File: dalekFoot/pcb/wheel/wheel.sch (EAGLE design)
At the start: 79 parts, among them IC1 LM1117MP-3.3, IC2 LM1117MP-3.3, IC3 LM1117MP-3.3, IC4 4051D, IC5 4051D, IC6 LM1117MP-3.3, K1 12X12-TACTILE, K2 12X12-TACTILE, K3 12X12-TACTILE, K4 12X12-TACTILE, K5 12X12-TACTILE, U1 TB6612FNG(O,C,8,EL, U2 SS8050-SOT-23, U3 SS8050-SOT-23, U4 SS8050-SOT-23, U5 TB6612FNG(O,C,8,EL, U6 TB6612FNG(O,C,8,EL

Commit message: add standalone usart port
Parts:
- added JP8: (no value), pinhead:PINHD-1X4
- added R36: (no value), rcl:R-EU_R0402
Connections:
- new net N$3: JP8.1, R36.2
- new net VCC-DIGITAL: B1.P$+, C2.+, IC1.OUT, JP5.1, JP5.2, JP6.1, JP6.2, LED1.A, LED2.A, R27.1, R28.1, R36.1, U$1.P$3V3, U1.STBY, U1.VCC, U5.STBY, U5.VCC, U6.STBY, U6.VCC
- net DGND: now also JP8.4
- net USART_RX: now also JP8.3
- net USART_TX: now also JP8.2
- net VCC-IRT: no longer B1.P$+, C2.+, IC1.OUT, JP5.1, JP5.2, JP6.1, JP6.2, LED1.A, LED2.A, R27.1, R28.1, U$1.P$3V3, U1.STBY, U1.VCC, U5.STBY, U5.VCC, U6.STBY, U6.VCC
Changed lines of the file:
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@@
 <setting verticaltext="up"/>
 </settings>
-<grid distance="0.1" unitdist="inch" unit="inch" style="lines" multiple="1" display="yes" altdistance="0.01" altunitdist="inch" altunit="inch"/>
+<grid distance="0.1" unitdist="inch" unit="inch" style="lines" multiple="1" display="no" altdistance="0.01" altunitdist="inch" altunit="inch"/>
 <layers>
 <layer number="1" name="Top" color="4" fill="1" visible="no" active="no"/>
@@
 <part name="U$2" library="hqc" deviceset="BATTERY-10A" device=""/>
 <part name="SUPPLY38" library="supply2" deviceset="DGND" device=""/>
+<part name="JP8" library="pinhead" deviceset="PINHD-1X4" device=""/>
+<part name="SUPPLY39" library="supply2" deviceset="DGND" device=""/>
+<part name="R36" library="rcl" deviceset="R-EU_" device="R0402"/>
 </parts>
 <sheets>
@@
 <instance part="U$2" gate="G$1" x="38.1" y="25.4"/>
 <instance part="SUPPLY38" gate="G$1" x="38.1" y="15.24"/>
+<instance part="JP8" gate="A" x="335.28" y="223.52"/>
+<instance part="SUPPLY39" gate="G$1" x="325.12" y="215.9"/>
+<instance part="R36" gate="G$1" x="312.42" y="228.6"/>
 </instances>
 <busses>
@@
 <wire x1="38.1" y1="20.32" x2="38.1" y2="17.78" width="0.1524" layer="91"/>
 </segment>
+<segment>
+<pinref part="SUPPLY39" gate="G$1" pin="DGND"/>
+<wire x1="325.12" y1="218.44" x2="325.12" y2="220.98" width="0.1524" layer="91"/>
+<pinref part="JP8" gate="A" pin="4"/>
+<wire x1="325.12" y1="220.98" x2="332.74" y2="220.98" width="0.1524" layer="91"/>
+</segment>
 </net>
 <net name="BAT+" class="0">
@@
 </segment>
 </net>
-<net name="VCC-IRT" class="0">
+<net name="VCC-DIGITAL" class="0">
 <segment>
 <pinref part="IC1" gate="G$1" pin="OUT"/>
@@
 </segment>
 <segment>
-<pinref part="IC6" gate="G$1" pin="OUT"/>
-<wire x1="162.56" y1="81.28" x2="170.18" y2="81.28" width="0.1524" layer="91"/>
-<pinref part="C9" gate="G$1" pin="+"/>
-<wire x1="170.18" y1="81.28" x2="182.88" y2="81.28" width="0.1524" layer="91"/>
-<wire x1="170.18" y1="76.2" x2="170.18" y2="81.28" width="0.1524" layer="91"/>
-<junction x="170.18" y="81.28"/>
-<label x="177.8" y="81.28" size="1.778" layer="95"/>
-</segment>
-<segment>
-<pinref part="R35" gate="G$1" pin="P$1"/>
-<wire x1="137.16" y1="38.1" x2="149.86" y2="38.1" width="0.1524" layer="91"/>
-<label x="134.62" y="38.1" size="1.778" layer="95"/>
+<wire x1="307.34" y1="228.6" x2="289.56" y2="228.6" width="0.1524" layer="91"/>
+<label x="289.56" y="228.6" size="1.778" layer="95"/>
+<pinref part="R36" gate="G$1" pin="1"/>
 </segment>
 </net>
@@
 <label x="274.32" y="259.08" size="1.778" layer="95"/>
 </segment>
+<segment>
+<pinref part="JP8" gate="A" pin="2"/>
+<wire x1="314.96" y1="226.06" x2="332.74" y2="226.06" width="0.1524" layer="91"/>
+<label x="314.96" y="226.06" size="1.778" layer="95"/>
+</segment>
 </net>
 <net name="USART_RX" class="0">
@@
 <label x="274.32" y="256.54" size="1.778" layer="95"/>
 </segment>
-</net>
+<segment>
+<pinref part="JP8" gate="A" pin="3"/>
+<wire x1="332.74" y1="223.52" x2="314.96" y2="223.52" width="0.1524" layer="91"/>
+<label x="314.96" y="223.52" size="1.778" layer="95"/>
+</segment>
+</net>
+<net name="N$3" class="0">
+<segment>
+<pinref part="JP8" gate="A" pin="1"/>
+<wire x1="332.74" y1="228.6" x2="317.5" y2="228.6" width="0.1524" layer="91"/>
+<pinref part="R36" gate="G$1" pin="2"/>
+</segment>
+</net>
+<net name="VCC-IRT" class="0">
+<segment>
+<pinref part="IC6" gate="G$1" pin="OUT"/>
+<wire x1="162.56" y1="81.28" x2="170.18" y2="81.28" width="0.1524" layer="91"/>
+<pinref part="C9" gate="G$1" pin="+"/>
+<wire x1="170.18" y1="81.28" x2="182.88" y2="81.28" width="0.1524" layer="91"/>
+<wire x1="170.18" y1="76.2" x2="170.18" y2="81.28" width="0.1524" layer="91"/>
+<junction x="170.18" y="81.28"/>
+<label x="177.8" y="81.28" size="1.778" layer="95"/>
+</segment>
+<segment>
+<pinref part="R35" gate="G$1" pin="P$1"/>
+<wire x1="137.16" y1="38.1" x2="149.86" y2="38.1" width="0.1524" layer="91"/>
+<label x="134.62" y="38.1" size="1.778" layer="95"/>
+</segment>
+</net>

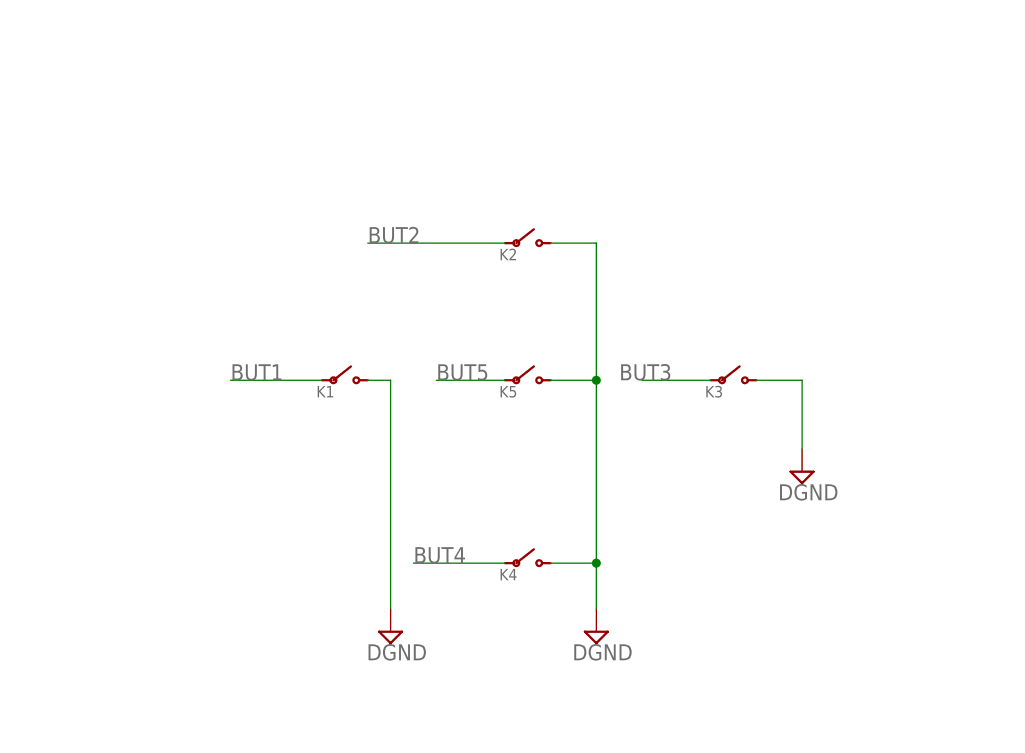
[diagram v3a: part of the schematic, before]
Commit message: place the parts in pcb, ready to route lines
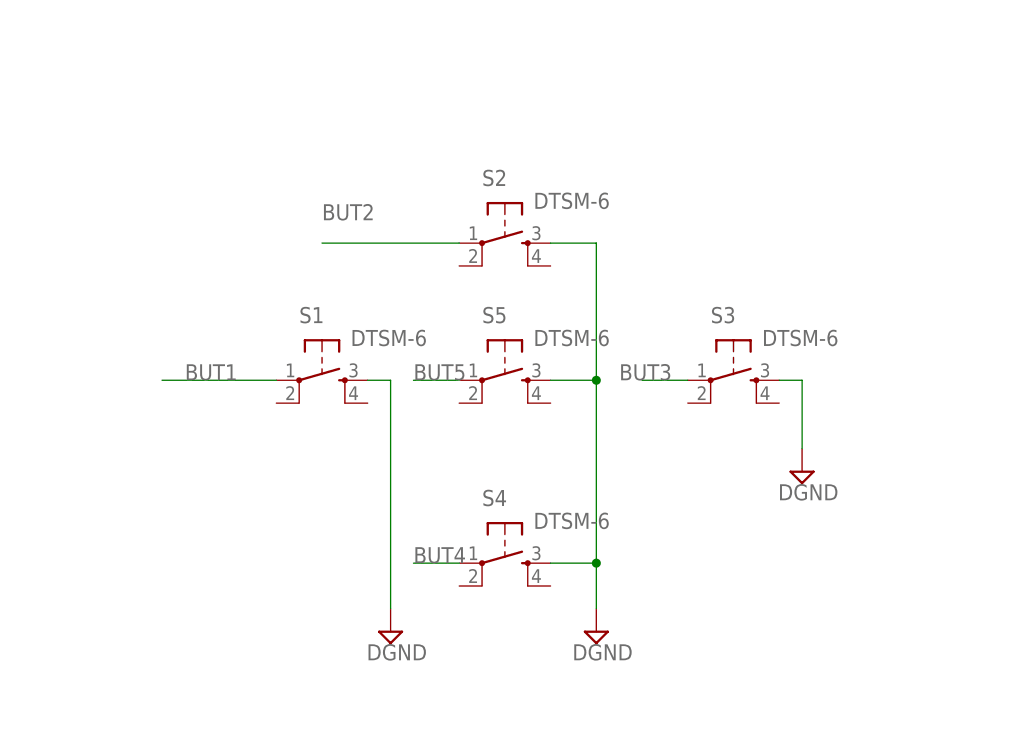
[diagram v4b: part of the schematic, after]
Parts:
- removed K1, K2, K3, K4, K5: 12X12-TACTILE, hqc:12X12-TACTILE
- added S1, S2, S3, S4, S5: DTSM-6, switch-tact:DTSM-6
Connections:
- net BUT1: now also S1.1; no longer K1.P$1
- net BUT2: now also S2.1; no longer K2.P$1
- net BUT3: now also S3.1; no longer K3.P$1
- net BUT4: now also S4.1; no longer K4.P$1
- net BUT5: now also S5.1; no longer K5.P$1
- net DGND: now also S1.3, S2.3, S3.3, S4.3, S5.3; no longer K1.P$2, K2.P$2, K3.P$2, K4.P$2, K5.P$2
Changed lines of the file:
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@@
 <setting verticaltext="up"/>
 </settings>
-<grid distance="0.1" unitdist="inch" unit="inch" style="lines" multiple="1" display="no" altdistance="0.01" altunitdist="inch" altunit="inch"/>
+<grid distance="0.1" unitdist="inch" unit="mil" style="lines" multiple="1" display="yes" altdistance="0.01" altunitdist="inch" altunit="inch"/>
 <layers>
 <layer number="1" name="Top" color="4" fill="1" visible="no" active="no"/>
@@
 <part name="J2" library="hqc" deviceset="KF250-2X12P" device=""/>
 <part name="SUPPLY30" library="supply2" deviceset="DGND" device=""/>
-<part name="K1" library="hqc" deviceset="12X12-TACTILE" device=""/>
-<part name="K2" library="hqc" deviceset="12X12-TACTILE" device=""/>
-<part name="K3" library="hqc" deviceset="12X12-TACTILE" device=""/>
-<part name="K4" library="hqc" deviceset="12X12-TACTILE" device=""/>
-<part name="K5" library="hqc" deviceset="12X12-TACTILE" device=""/>
 <part name="SUPPLY31" library="supply2" deviceset="DGND" device=""/>
 <part name="SUPPLY32" library="supply2" deviceset="DGND" device=""/>
@@
 <part name="SUPPLY39" library="supply2" deviceset="DGND" device=""/>
 <part name="R36" library="rcl" deviceset="R-EU_" device="R0402"/>
+<part name="S1" library="switch-tact" deviceset="DTSM-6" device=""/>
+<part name="S2" library="switch-tact" deviceset="DTSM-6" device=""/>
+<part name="S3" library="switch-tact" deviceset="DTSM-6" device=""/>
+<part name="S4" library="switch-tact" deviceset="DTSM-6" device=""/>
+<part name="S5" library="switch-tact" deviceset="DTSM-6" device=""/>
 </parts>
 <sheets>
@@
 <instance part="J2" gate="G$1" x="365.76" y="596.9" rot="R270"/>
 <instance part="SUPPLY30" gate="G$1" x="353.06" y="568.96"/>
-<instance part="K1" gate="G$1" x="78.74" y="375.92"/>
-<instance part="K2" gate="G$1" x="99.06" y="391.16"/>
-<instance part="K3" gate="G$1" x="121.92" y="375.92"/>
-<instance part="K4" gate="G$1" x="99.06" y="355.6"/>
-<instance part="K5" gate="G$1" x="99.06" y="375.92"/>
 <instance part="SUPPLY31" gate="G$1" x="106.68" y="347.98"/>
 <instance part="SUPPLY32" gate="G$1" x="83.82" y="347.98"/>
@@
 <instance part="SUPPLY39" gate="G$1" x="325.12" y="215.9"/>
 <instance part="R36" gate="G$1" x="312.42" y="228.6"/>
+<instance part="S1" gate="G$1" x="76.2" y="375.92" rot="R270"/>
+<instance part="S2" gate="G$1" x="96.52" y="391.16" rot="R270"/>
+<instance part="S3" gate="G$1" x="121.92" y="375.92" rot="R270"/>
+<instance part="S4" gate="G$1" x="96.52" y="355.6" rot="R270"/>
+<instance part="S5" gate="G$1" x="96.52" y="375.92" rot="R270"/>
 </instances>
 <busses>
@@
 </segment>
 <segment>
-<pinref part="K4" gate="G$1" pin="P$2"/>
 <wire x1="101.6" y1="355.6" x2="106.68" y2="355.6" width="0.1524" layer="91"/>
 <pinref part="SUPPLY31" gate="G$1" pin="DGND"/>
 <wire x1="106.68" y1="355.6" x2="106.68" y2="350.52" width="0.1524" layer="91"/>
-<pinref part="K5" gate="G$1" pin="P$2"/>
 <wire x1="101.6" y1="375.92" x2="106.68" y2="375.92" width="0.1524" layer="91"/>
 <wire x1="106.68" y1="375.92" x2="106.68" y2="355.6" width="0.1524" layer="91"/>
 <junction x="106.68" y="355.6"/>
-<pinref part="K2" gate="G$1" pin="P$2"/>
 <wire x1="101.6" y1="391.16" x2="106.68" y2="391.16" width="0.1524" layer="91"/>
 <wire x1="106.68" y1="391.16" x2="106.68" y2="375.92" width="0.1524" layer="91"/>
 <junction x="106.68" y="375.92"/>
-</segment>
-<segment>
-<pinref part="K1" gate="G$1" pin="P$2"/>
+<pinref part="S2" gate="G$1" pin="3"/>
+<pinref part="S5" gate="G$1" pin="3"/>
+<pinref part="S4" gate="G$1" pin="3"/>
+</segment>
+<segment>
 <wire x1="81.28" y1="375.92" x2="83.82" y2="375.92" width="0.1524" layer="91"/>
 <wire x1="83.82" y1="375.92" x2="83.82" y2="350.52" width="0.1524" layer="91"/>
 <pinref part="SUPPLY32" gate="G$1" pin="DGND"/>
-</segment>
-<segment>
-<pinref part="K3" gate="G$1" pin="P$2"/>
-<wire x1="124.46" y1="375.92" x2="129.54" y2="375.92" width="0.1524" layer="91"/>
+<pinref part="S1" gate="G$1" pin="3"/>
+</segment>
+<segment>
+<wire x1="127" y1="375.92" x2="129.54" y2="375.92" width="0.1524" layer="91"/>
 <wire x1="129.54" y1="375.92" x2="129.54" y2="368.3" width="0.1524" layer="91"/>
 <pinref part="SUPPLY33" gate="G$1" pin="DGND"/>
+<pinref part="S3" gate="G$1" pin="3"/>
 </segment>
 <segment>
@@
 </segment>
 <segment>
-<pinref part="K1" gate="G$1" pin="P$1"/>
-<wire x1="76.2" y1="375.92" x2="66.04" y2="375.92" width="0.1524" layer="91"/>
-<label x="66.04" y="375.92" size="1.778" layer="95"/>
+<wire x1="71.12" y1="375.92" x2="58.42" y2="375.92" width="0.1524" layer="91"/>
+<label x="60.96" y="375.92" size="1.778" layer="95"/>
+<pinref part="S1" gate="G$1" pin="1"/>
 </segment>
 </net>
@@
 </segment>
 <segment>
-<pinref part="K2" gate="G$1" pin="P$1"/>
-<wire x1="96.52" y1="391.16" x2="81.28" y2="391.16" width="0.1524" layer="91"/>
-<label x="81.28" y="391.16" size="1.778" layer="95"/>
+<wire x1="91.44" y1="391.16" x2="76.2" y2="391.16" width="0.1524" layer="91"/>
+<label x="76.2" y="393.7" size="1.778" layer="95"/>
+<pinref part="S2" gate="G$1" pin="1"/>
 </segment>
 </net>
@@
 </segment>
 <segment>
-<pinref part="K3" gate="G$1" pin="P$1"/>
-<wire x1="111.76" y1="375.92" x2="119.38" y2="375.92" width="0.1524" layer="91"/>
+<wire x1="111.76" y1="375.92" x2="116.84" y2="375.92" width="0.1524" layer="91"/>
 <label x="109.22" y="375.92" size="1.778" layer="95"/>
+<pinref part="S3" gate="G$1" pin="1"/>
 </segment>
 </net>
@@
 </segment>
 <segment>
-<pinref part="K4" gate="G$1" pin="P$1"/>
-<wire x1="86.36" y1="355.6" x2="96.52" y2="355.6" width="0.1524" layer="91"/>
+<wire x1="86.36" y1="355.6" x2="91.44" y2="355.6" width="0.1524" layer="91"/>
 <label x="86.36" y="355.6" size="1.778" layer="95"/>
+<pinref part="S4" gate="G$1" pin="1"/>
 </segment>
 </net>
@@
 </segment>
 <segment>
-<pinref part="K5" gate="G$1" pin="P$1"/>
-<wire x1="96.52" y1="375.92" x2="88.9" y2="375.92" width="0.1524" layer="91"/>
-<label x="88.9" y="375.92" size="1.778" layer="95"/>
-</segment>
-</net>
+<wire x1="91.44" y1="375.92" x2="86.36" y2="375.92" width="0.1524" layer="91"/>
+<label x="86.36" y="375.92" size="1.778" layer="95"/>
+<pinref part="S5" gate="G$1" pin="1"/>
+</segment>
+</net>
